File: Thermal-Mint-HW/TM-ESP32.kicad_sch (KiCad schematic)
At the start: 32 parts, among them SW1 PTS647, SW2 PTS647, U3 SN74LVC138ARSVR, U4 AT25DL081-SSHN-T, U7 ESP32-C3, Y1 FL4000157Z

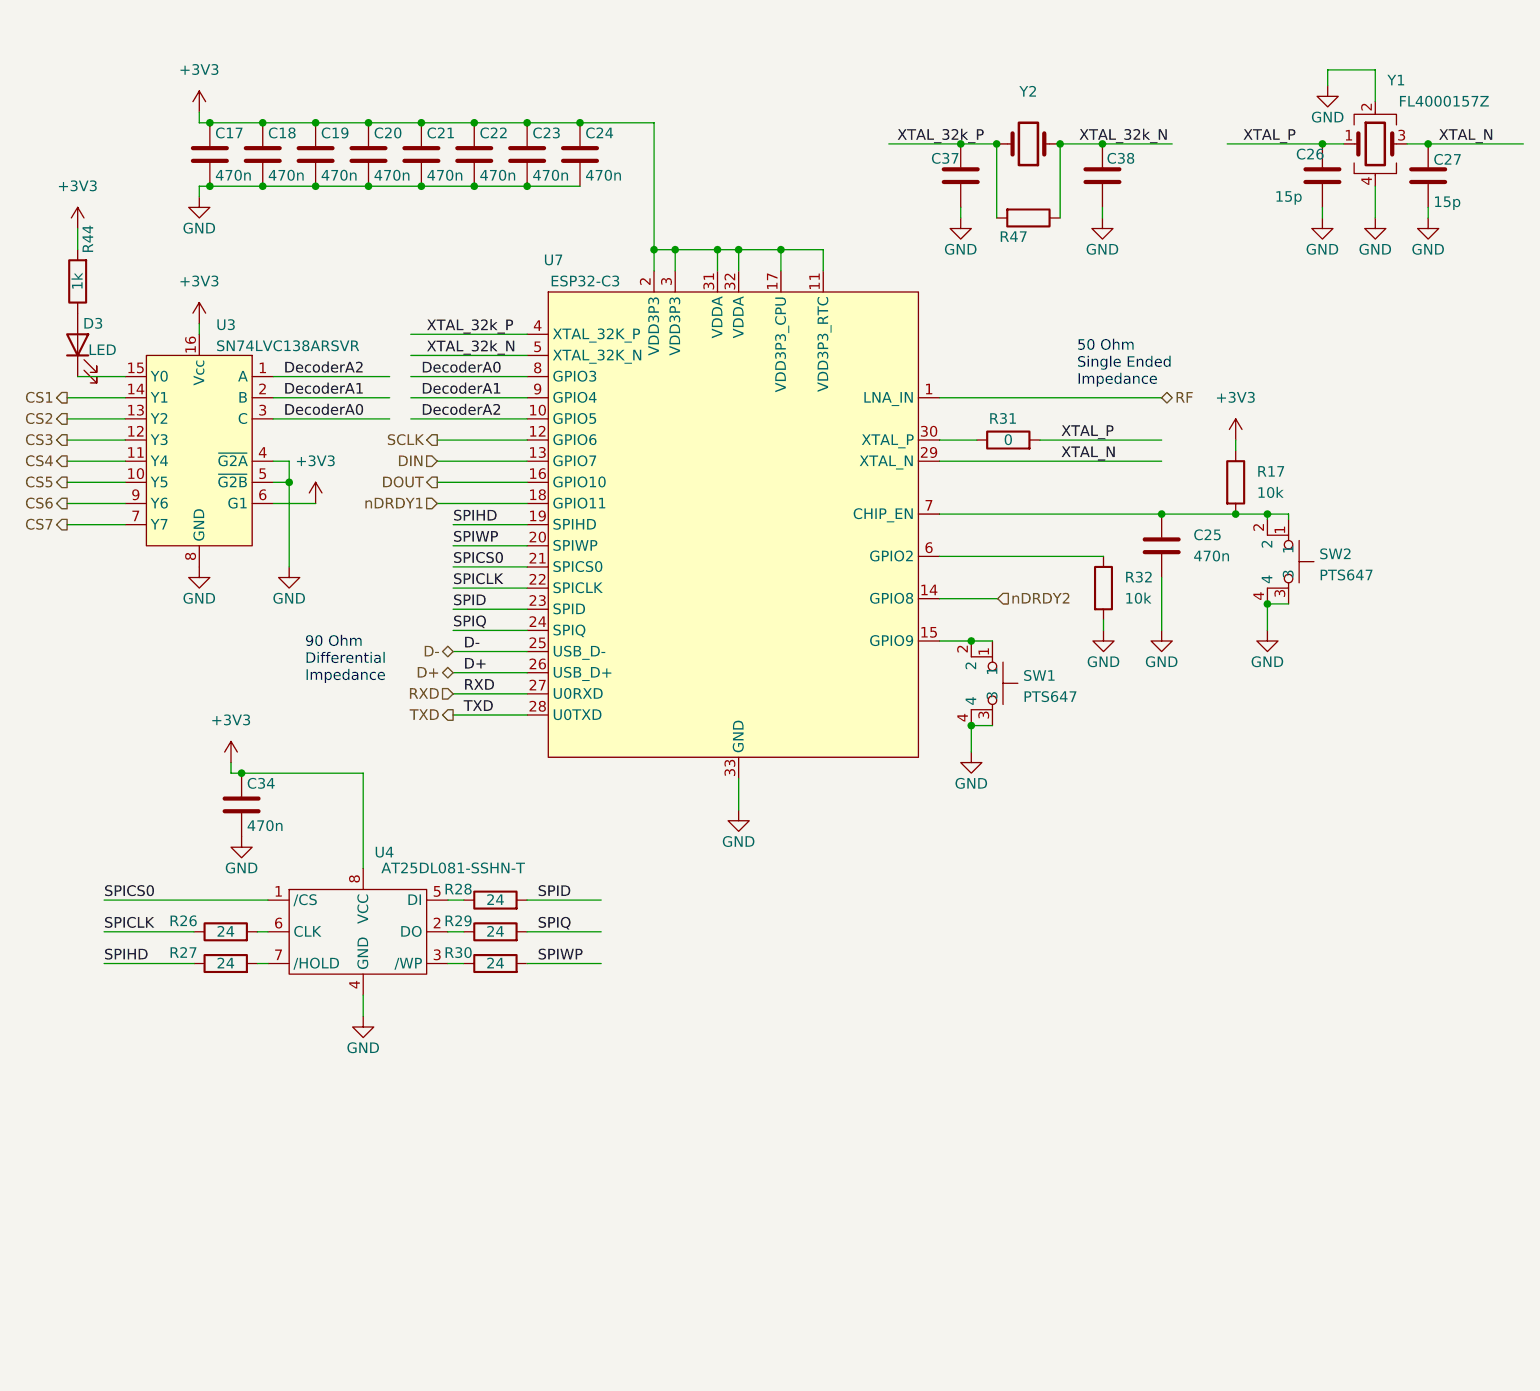
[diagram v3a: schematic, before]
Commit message: Temporary commit before changing processor from C3 to s2
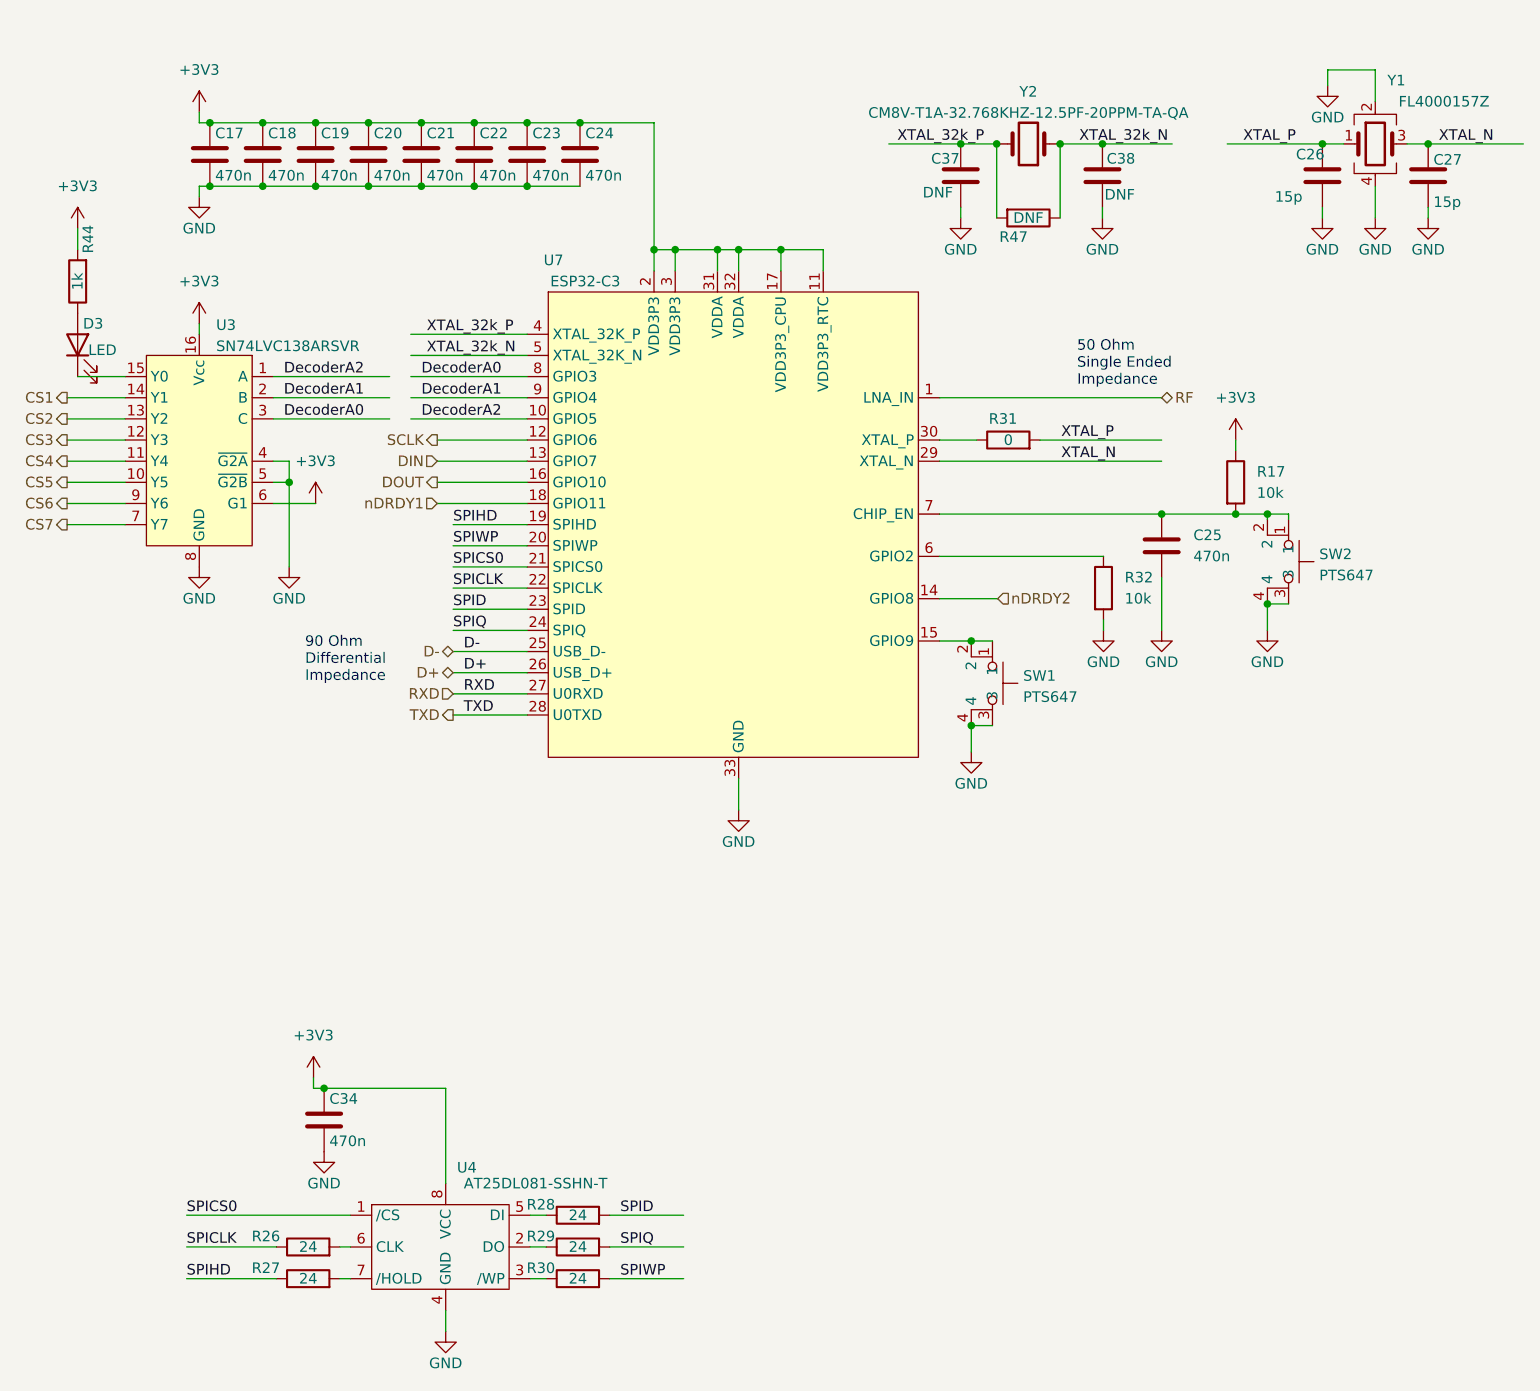
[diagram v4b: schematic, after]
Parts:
- C37, C38, R47: value (none) -> DNF
- Y2: value (none) -> CM8V-T1A-32.768KHZ-12.5PF-20PPM-TA-QA; footprint (none) -> Crystal:Crystal_SMD_TXC_9HT11-2Pin_2.0x1.2mm_HandSoldering
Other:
- title: (none) -> Thermal Mint
- moved on the sheet: C34, R26, R27, R28, R29, R30, U4
